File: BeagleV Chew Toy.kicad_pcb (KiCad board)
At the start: 2 copper layers, 41.1 x 51.1 mm, 3 parts

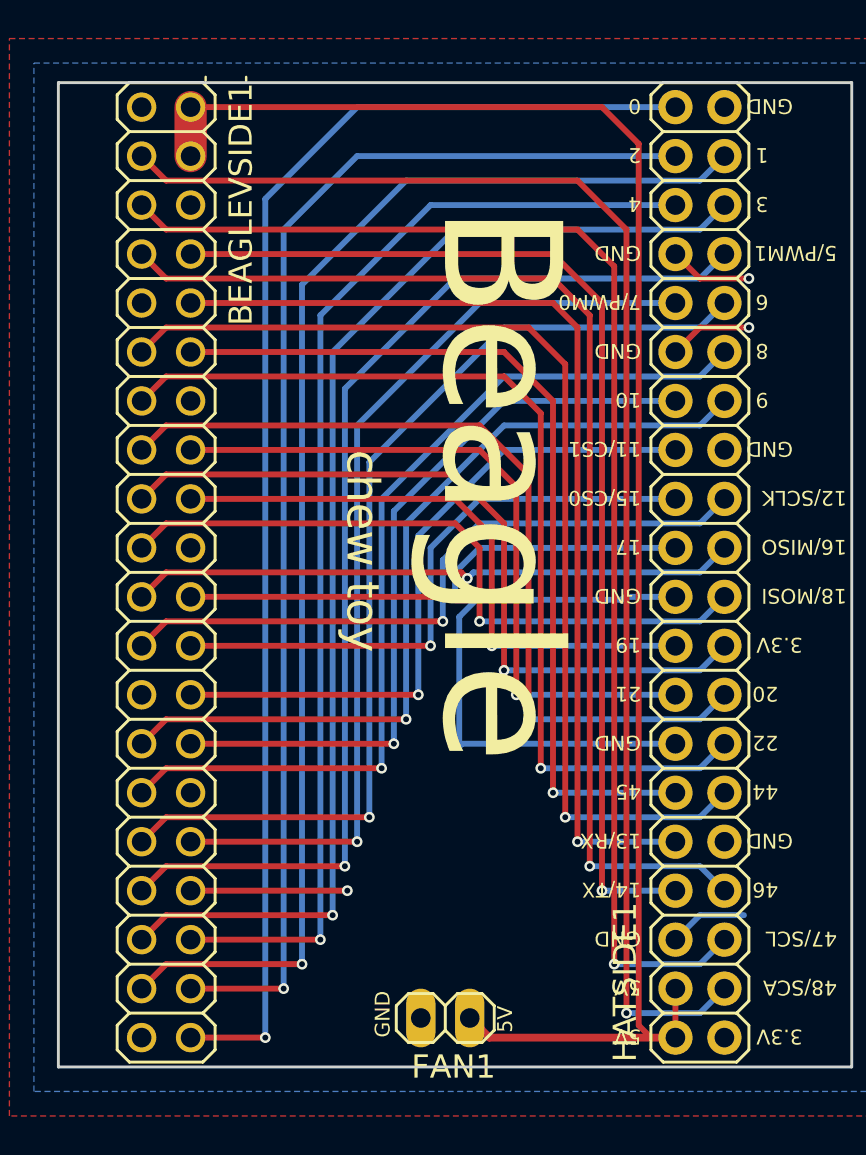
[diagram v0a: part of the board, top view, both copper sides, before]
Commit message: replace connectors
The footprints aren't the same anyway so let's use the Kicad parts.
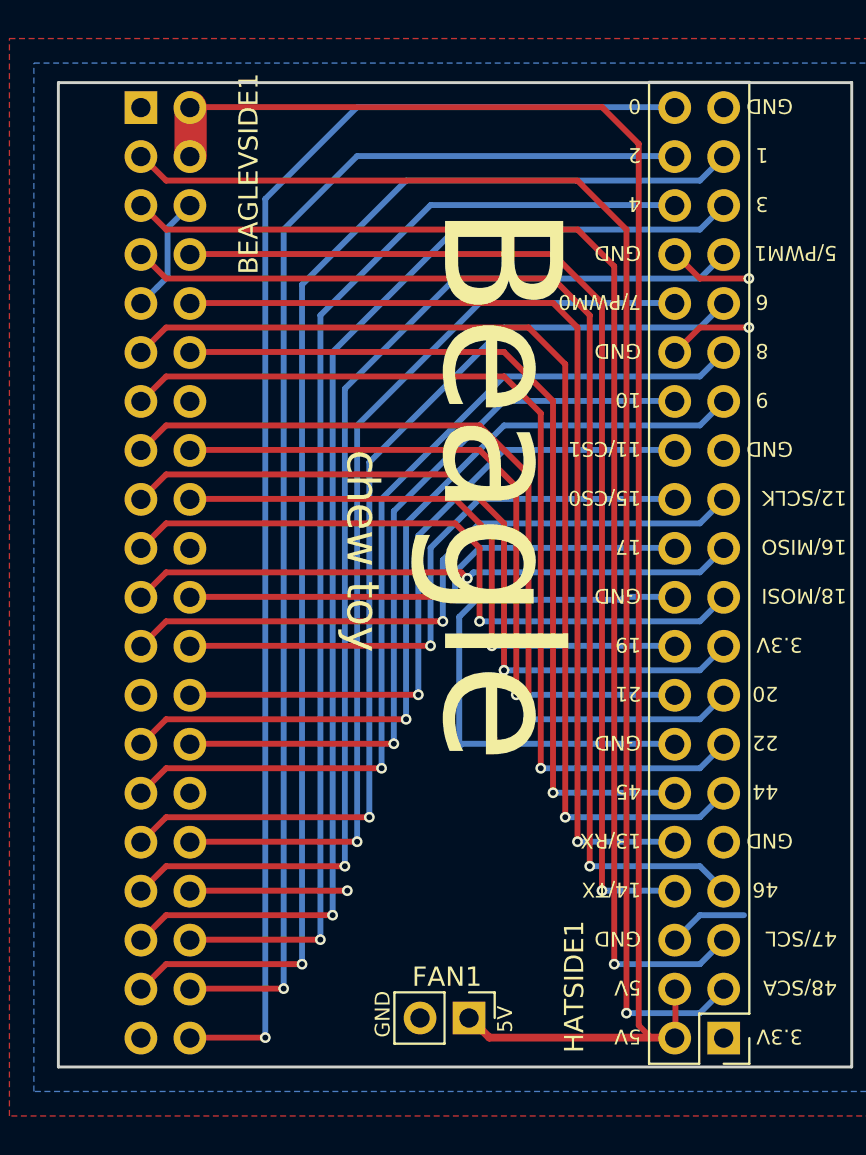
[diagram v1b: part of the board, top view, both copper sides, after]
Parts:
- BEAGLEVSIDE1: footprint BeagleV Chew Toy:2X20 -> Connector_PinSocket_2.54mm:PinSocket_2x20_P2.54mm_Vertical; moved to B.Cu
- FAN1: footprint BeagleV Chew Toy:1X02 -> Connector_PinHeader_2.54mm:PinHeader_1x02_P2.54mm_Vertical
- HATSIDE1: footprint BeagleV Chew Toy:2X20-BIG -> Connector_PinHeader_2.54mm:PinHeader_2x20_P2.54mm_Vertical
- moved HATSIDE1 24.2 mm to (162.4, 129.0), turned to 180 degrees
- moved BEAGLEVSIDE1 24.1 mm to (132.2, 80.8), turned to 180 degrees
- moved FAN1 1.23 mm to (149.2, 128.0), turned to 270 degrees
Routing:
- net /GND: track 50.5 -> 56.6 mm

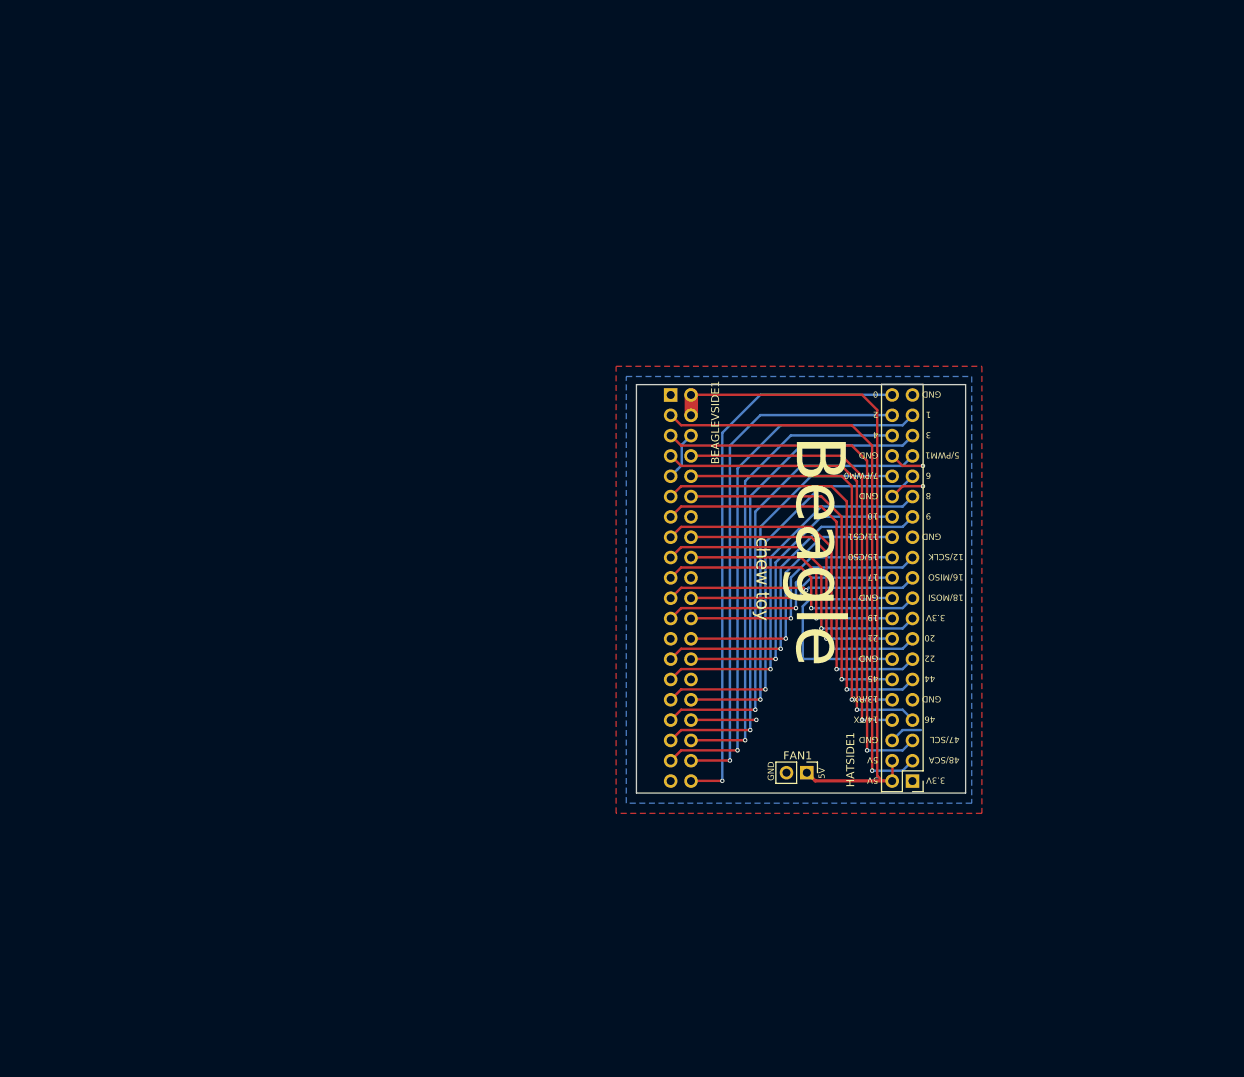
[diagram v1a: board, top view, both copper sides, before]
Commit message: add most of the parts that we need
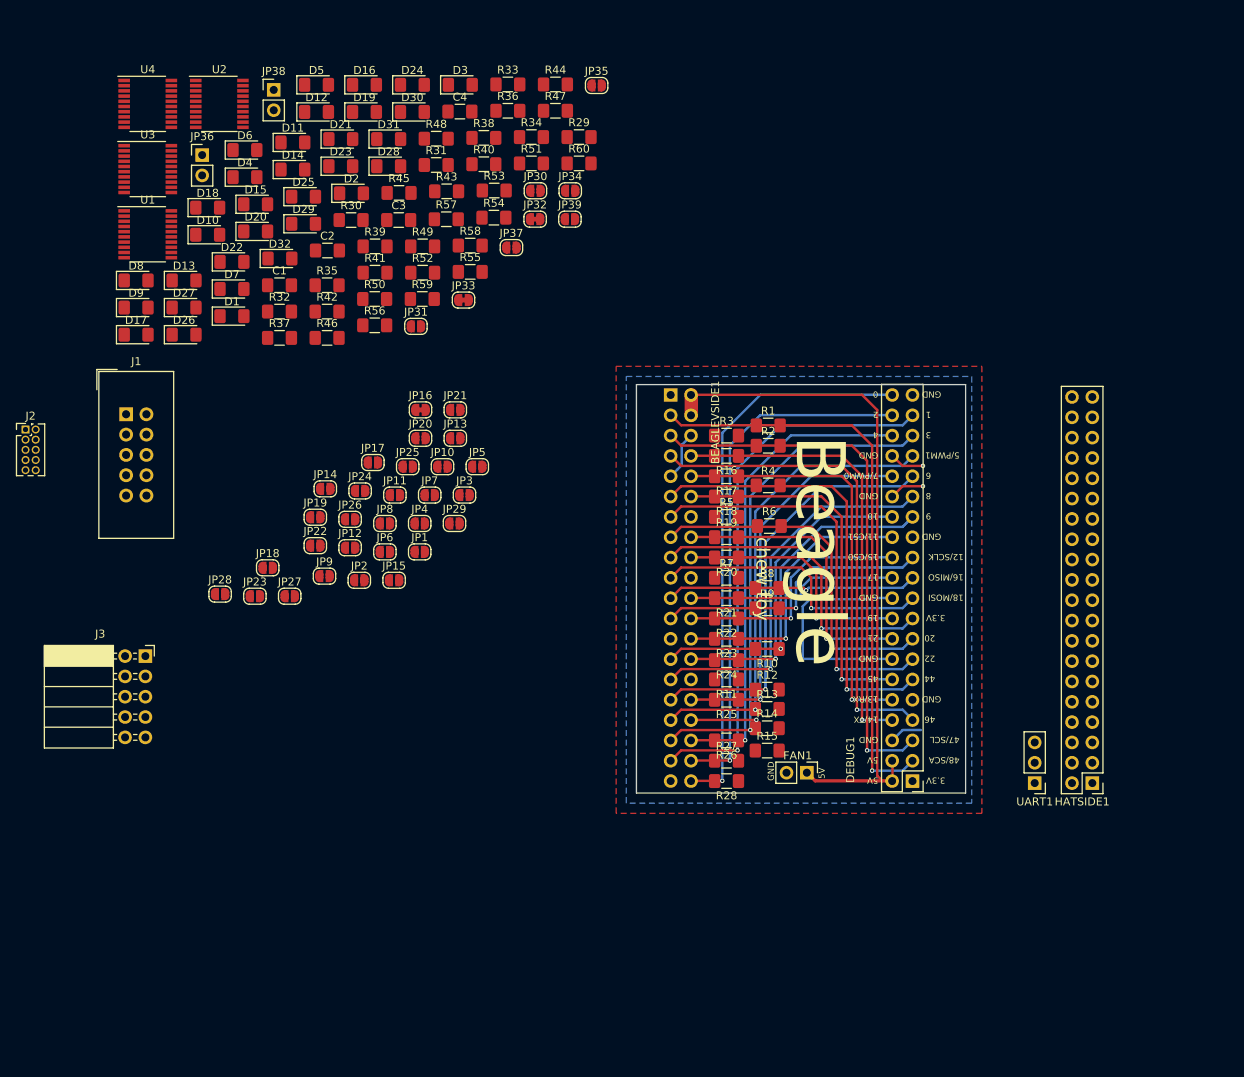
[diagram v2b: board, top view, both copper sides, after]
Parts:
- added C1: 100n, Capacitor_SMD:C_1206_3216Metric_Pad1.42x1.75mm_HandSolder, F.Cu at (83.3, 67.1)
- added C2: 100n, Capacitor_SMD:C_1206_3216Metric_Pad1.42x1.75mm_HandSolder, F.Cu at (89.3, 62.7)
- added C3: 100n, Capacitor_SMD:C_1206_3216Metric_Pad1.42x1.75mm_HandSolder, F.Cu at (98.2, 58.9)
- added C4: 100n, Capacitor_SMD:C_1206_3216Metric_Pad1.42x1.75mm_HandSolder, F.Cu at (105.9, 45.3)
- added D1: LED, LED_SMD:LED_1206_3216Metric_Pad1.42x1.75mm_HandSolder, F.Cu at (77.4, 70.9)
- added D10: LED, LED_SMD:LED_1206_3216Metric_Pad1.42x1.75mm_HandSolder, F.Cu at (74.3, 60.7)
- added D11: LED, LED_SMD:LED_1206_3216Metric_Pad1.42x1.75mm_HandSolder, F.Cu at (85.0, 49.2)
- added D12: LED, LED_SMD:LED_1206_3216Metric_Pad1.42x1.75mm_HandSolder, F.Cu at (87.9, 45.4)
- added D13: LED, LED_SMD:LED_1206_3216Metric_Pad1.42x1.75mm_HandSolder, F.Cu at (71.4, 66.5)
- added D14: LED, LED_SMD:LED_1206_3216Metric_Pad1.42x1.75mm_HandSolder, F.Cu at (85.0, 52.6)
- added D15: LED, LED_SMD:LED_1206_3216Metric_Pad1.42x1.75mm_HandSolder, F.Cu at (80.3, 56.9)
- added D16: LED, LED_SMD:LED_1206_3216Metric_Pad1.42x1.75mm_HandSolder, F.Cu at (93.9, 42.0)
- added D17: LED, LED_SMD:LED_1206_3216Metric_Pad1.42x1.75mm_HandSolder, F.Cu at (65.4, 73.2)
- added D18: LED, LED_SMD:LED_1206_3216Metric_Pad1.42x1.75mm_HandSolder, F.Cu at (74.3, 57.4)
- added D19: LED, LED_SMD:LED_1206_3216Metric_Pad1.42x1.75mm_HandSolder, F.Cu at (93.9, 45.4)
- added D2: LED, LED_SMD:LED_1206_3216Metric_Pad1.42x1.75mm_HandSolder, F.Cu at (92.3, 55.6)
- added D20: LED, LED_SMD:LED_1206_3216Metric_Pad1.42x1.75mm_HandSolder, F.Cu at (80.3, 60.3)
- added D21: LED, LED_SMD:LED_1206_3216Metric_Pad1.42x1.75mm_HandSolder, F.Cu at (91.0, 48.8)
- added D22: LED, LED_SMD:LED_1206_3216Metric_Pad1.42x1.75mm_HandSolder, F.Cu at (77.4, 64.1)
- added D23: LED, LED_SMD:LED_1206_3216Metric_Pad1.42x1.75mm_HandSolder, F.Cu at (91.0, 52.2)
- added D24: LED, LED_SMD:LED_1206_3216Metric_Pad1.42x1.75mm_HandSolder, F.Cu at (99.9, 42.0)
- added D25: LED, LED_SMD:LED_1206_3216Metric_Pad1.42x1.75mm_HandSolder, F.Cu at (86.3, 56.0)
- added D26: LED, LED_SMD:LED_1206_3216Metric_Pad1.42x1.75mm_HandSolder, F.Cu at (71.4, 73.2)
- added D27: LED, LED_SMD:LED_1206_3216Metric_Pad1.42x1.75mm_HandSolder, F.Cu at (71.4, 69.8)
- added D28: LED, LED_SMD:LED_1206_3216Metric_Pad1.42x1.75mm_HandSolder, F.Cu at (97.0, 52.2)
- added D29: LED, LED_SMD:LED_1206_3216Metric_Pad1.42x1.75mm_HandSolder, F.Cu at (86.3, 59.4)
- added D3: LED, LED_SMD:LED_1206_3216Metric_Pad1.42x1.75mm_HandSolder, F.Cu at (105.9, 42.0)
- added D30: LED, LED_SMD:LED_1206_3216Metric_Pad1.42x1.75mm_HandSolder, F.Cu at (99.9, 45.4)
- added D31: LED, LED_SMD:LED_1206_3216Metric_Pad1.42x1.75mm_HandSolder, F.Cu at (97.0, 48.8)
- added D32: LED, LED_SMD:LED_1206_3216Metric_Pad1.42x1.75mm_HandSolder, F.Cu at (83.4, 63.7)
- added D4: LED, LED_SMD:LED_1206_3216Metric_Pad1.42x1.75mm_HandSolder, F.Cu at (79.0, 53.5)
- added D5: LED, LED_SMD:LED_1206_3216Metric_Pad1.42x1.75mm_HandSolder, F.Cu at (87.9, 42.0)
- added D6: LED, LED_SMD:LED_1206_3216Metric_Pad1.42x1.75mm_HandSolder, F.Cu at (79.0, 50.2)
- added D7: LED, LED_SMD:LED_1206_3216Metric_Pad1.42x1.75mm_HandSolder, F.Cu at (77.4, 67.5)
- added D8: LED, LED_SMD:LED_1206_3216Metric_Pad1.42x1.75mm_HandSolder, F.Cu at (65.4, 66.5)
- added D9: LED, LED_SMD:LED_1206_3216Metric_Pad1.42x1.75mm_HandSolder, F.Cu at (65.4, 69.8)
- added HATSIDE1: PINHD-2X20-BIG, Connector_PinHeader_2.54mm:PinHeader_2x20_P2.54mm_Vertical, F.Cu at (184.9, 129.3)
- added J1: Conn_02x05_Counter_Clockwise, Connector_IDC:IDC-Header_2x05_P2.54mm_Vertical, F.Cu at (64.1, 83.2)
- added J2: Conn_02x05_Counter_Clockwise, Connector_PinHeader_1.27mm:PinHeader_2x05_P1.27mm_Vertical, F.Cu at (51.6, 85.1)
- added J3: Conn_02x05_Counter_Clockwise, Connector_PinSocket_2.54mm:PinSocket_2x05_P2.54mm_Horizontal, F.Cu at (66.5, 113.4)
- added JP1: SolderJumper_2_Bridged, Jumper:SolderJumper-2_P1.3mm_Open_RoundedPad1.0x1.5mm, F.Cu at (100.8, 100.4)
- added JP10: SolderJumper_2_Bridged, Jumper:SolderJumper-2_P1.3mm_Open_RoundedPad1.0x1.5mm, F.Cu at (103.7, 89.7)
- added JP11: SolderJumper_2_Bridged, Jumper:SolderJumper-2_P1.3mm_Open_RoundedPad1.0x1.5mm, F.Cu at (97.7, 93.3)
- added JP12: SolderJumper_2_Bridged, Jumper:SolderJumper-2_P1.3mm_Open_RoundedPad1.0x1.5mm, F.Cu at (92.1, 99.9)
- added JP13: SolderJumper_2_Bridged, Jumper:SolderJumper-2_P1.3mm_Open_RoundedPad1.0x1.5mm, F.Cu at (105.3, 86.2)
- added JP14: SolderJumper_2_Bridged, Jumper:SolderJumper-2_P1.3mm_Open_RoundedPad1.0x1.5mm, F.Cu at (89.0, 92.5)
- added JP15: SolderJumper_2_Bridged, Jumper:SolderJumper-2_P1.3mm_Open_RoundedPad1.0x1.5mm, F.Cu at (97.6, 103.9)
- added JP16: SolderJumper_2_Bridged, Jumper:SolderJumper-2_P1.3mm_Bridged_RoundedPad1.0x1.5mm, F.Cu at (100.9, 82.6)
- added JP17: SolderJumper_2_Bridged, Jumper:SolderJumper-2_P1.3mm_Open_RoundedPad1.0x1.5mm, F.Cu at (95.0, 89.2)
- added JP18: SolderJumper_2_Bridged, Jumper:SolderJumper-2_P1.3mm_Open_RoundedPad1.0x1.5mm, F.Cu at (81.8, 102.4)
- added JP19: SolderJumper_2_Bridged, Jumper:SolderJumper-2_P1.3mm_Open_RoundedPad1.0x1.5mm, F.Cu at (87.8, 96.1)
- added JP2: SolderJumper_2_Bridged, Jumper:SolderJumper-2_P1.3mm_Open_RoundedPad1.0x1.5mm, F.Cu at (93.3, 103.9)
- added JP20: SolderJumper_2_Bridged, Jumper:SolderJumper-2_P1.3mm_Open_RoundedPad1.0x1.5mm, F.Cu at (100.9, 86.2)
- added JP21: SolderJumper_2_Bridged, Jumper:SolderJumper-2_P1.3mm_Open_RoundedPad1.0x1.5mm, F.Cu at (105.3, 82.6)
- added JP22: SolderJumper_2_Bridged, Jumper:SolderJumper-2_P1.3mm_Open_RoundedPad1.0x1.5mm, F.Cu at (87.8, 99.6)
- added JP23: SolderJumper_2_Bridged, Jumper:SolderJumper-2_P1.3mm_Open_RoundedPad1.0x1.5mm, F.Cu at (80.2, 105.9)
- added JP24: SolderJumper_2_Bridged, Jumper:SolderJumper-2_P1.3mm_Open_RoundedPad1.0x1.5mm, F.Cu at (93.4, 92.8)
- added JP25: SolderJumper_2_Bridged, Jumper:SolderJumper-2_P1.3mm_Open_RoundedPad1.0x1.5mm, F.Cu at (99.3, 89.7)
- added JP26: SolderJumper_2_Bridged, Jumper:SolderJumper-2_P1.3mm_Open_RoundedPad1.0x1.5mm, F.Cu at (92.1, 96.3)
- added JP27: SolderJumper_2_Bridged, Jumper:SolderJumper-2_P1.3mm_Open_RoundedPad1.0x1.5mm, F.Cu at (84.6, 105.9)
- added JP28: SolderJumper_2_Bridged, Jumper:SolderJumper-2_P1.3mm_Open_RoundedPad1.0x1.5mm, F.Cu at (75.9, 105.7)
- added JP29: SolderJumper_2_Bridged, Jumper:SolderJumper-2_P1.3mm_Open_RoundedPad1.0x1.5mm, F.Cu at (105.2, 96.8)
- added JP3: SolderJumper_2_Bridged, Jumper:SolderJumper-2_P1.3mm_Open_RoundedPad1.0x1.5mm, F.Cu at (106.4, 93.3)
- added JP30: SolderJumper_2_Bridged, Jumper:SolderJumper-2_P1.3mm_Open_RoundedPad1.0x1.5mm, F.Cu at (115.3, 55.2)
- added JP31: SolderJumper_2_Bridged, Jumper:SolderJumper-2_P1.3mm_Open_RoundedPad1.0x1.5mm, F.Cu at (100.4, 72.2)
- added JP32: SolderJumper_2_Bridged, Jumper:SolderJumper-2_P1.3mm_Bridged_RoundedPad1.0x1.5mm, F.Cu at (115.3, 58.8)
- added JP33: SolderJumper_2_Bridged, Jumper:SolderJumper-2_P1.3mm_Bridged_RoundedPad1.0x1.5mm, F.Cu at (106.3, 68.9)
- added JP34: SolderJumper_2_Bridged, Jumper:SolderJumper-2_P1.3mm_Open_RoundedPad1.0x1.5mm, F.Cu at (119.7, 55.2)
- added JP35: SolderJumper_2_Bridged, Jumper:SolderJumper-2_P1.3mm_Open_RoundedPad1.0x1.5mm, F.Cu at (123.0, 42.1)
- added JP36: Jumper, Connector_PinHeader_2.54mm:PinHeader_1x02_P2.54mm_Vertical, F.Cu at (73.6, 50.8)
- added JP37: SolderJumper_2_Bridged, Jumper:SolderJumper-2_P1.3mm_Open_RoundedPad1.0x1.5mm, F.Cu at (112.3, 62.3)
- added JP38: Jumper, Connector_PinHeader_2.54mm:PinHeader_1x02_P2.54mm_Vertical, F.Cu at (82.6, 42.6)
- added JP39: SolderJumper_2_Bridged, Jumper:SolderJumper-2_P1.3mm_Open_RoundedPad1.0x1.5mm, F.Cu at (119.6, 58.8)
- added JP4: SolderJumper_2_Bridged, Jumper:SolderJumper-2_P1.3mm_Open_RoundedPad1.0x1.5mm, F.Cu at (100.8, 96.8)
- added JP5: SolderJumper_2_Bridged, Jumper:SolderJumper-2_P1.3mm_Open_RoundedPad1.0x1.5mm, F.Cu at (108.0, 89.7)
- added JP6: SolderJumper_2_Bridged, Jumper:SolderJumper-2_P1.3mm_Open_RoundedPad1.0x1.5mm, F.Cu at (96.5, 100.4)
- added JP7: SolderJumper_2_Bridged, Jumper:SolderJumper-2_P1.3mm_Open_RoundedPad1.0x1.5mm, F.Cu at (102.1, 93.3)
- added JP8: SolderJumper_2_Bridged, Jumper:SolderJumper-2_P1.3mm_Open_RoundedPad1.0x1.5mm, F.Cu at (96.5, 96.8)
- added JP9: SolderJumper_2_Bridged, Jumper:SolderJumper-2_P1.3mm_Open_RoundedPad1.0x1.5mm, F.Cu at (88.9, 103.4)
- added R1: 100R, Resistor_SMD:R_1206_3216Metric_Pad1.42x1.75mm_HandSolder, F.Cu at (144.4, 84.6)
- added R10: 100R, Resistor_SMD:R_1206_3216Metric_Pad1.42x1.75mm_HandSolder, F.Cu at (144.3, 112.5)
- added R11: 100R, Resistor_SMD:R_1206_3216Metric_Pad1.42x1.75mm_HandSolder, F.Cu at (139.2, 116.3)
- added R12: 100R, Resistor_SMD:R_1206_3216Metric_Pad1.42x1.75mm_HandSolder, F.Cu at (144.3, 117.6)
- added R13: 100R, Resistor_SMD:R_1206_3216Metric_Pad1.42x1.75mm_HandSolder, F.Cu at (144.3, 120.0)
- added R14: 100R, Resistor_SMD:R_1206_3216Metric_Pad1.42x1.75mm_HandSolder, F.Cu at (144.3, 122.4)
- added R15: 100R, Resistor_SMD:R_1206_3216Metric_Pad1.42x1.75mm_HandSolder, F.Cu at (144.3, 125.2)
- added R16: 100R, Resistor_SMD:R_1206_3216Metric_Pad1.42x1.75mm_HandSolder, F.Cu at (139.2, 88.4)
- added R17: 100R, Resistor_SMD:R_1206_3216Metric_Pad1.42x1.75mm_HandSolder, F.Cu at (139.2, 90.9)
- added R18: 100R, Resistor_SMD:R_1206_3216Metric_Pad1.42x1.75mm_HandSolder, F.Cu at (139.2, 93.5)
- added R19: 100R, Resistor_SMD:R_1206_3216Metric_Pad1.42x1.75mm_HandSolder, F.Cu at (139.2, 98.6)
- added R2: 100R, Resistor_SMD:R_1206_3216Metric_Pad1.42x1.75mm_HandSolder, F.Cu at (144.4, 87.1)
- added R20: 100R, Resistor_SMD:R_1206_3216Metric_Pad1.42x1.75mm_HandSolder, F.Cu at (139.2, 101.1)
- added R21: 100R, Resistor_SMD:R_1206_3216Metric_Pad1.42x1.75mm_HandSolder, F.Cu at (139.2, 106.2)
- added R22: 100R, Resistor_SMD:R_1206_3216Metric_Pad1.42x1.75mm_HandSolder, F.Cu at (139.2, 108.7)
- added R23: 100R, Resistor_SMD:R_1206_3216Metric_Pad1.42x1.75mm_HandSolder, F.Cu at (139.2, 111.3)
- added R24: 100R, Resistor_SMD:R_1206_3216Metric_Pad1.42x1.75mm_HandSolder, F.Cu at (139.2, 113.9)
- added R25: 100R, Resistor_SMD:R_1206_3216Metric_Pad1.42x1.75mm_HandSolder, F.Cu at (139.2, 118.9)
- added R26: 100R, Resistor_SMD:R_1206_3216Metric_Pad1.42x1.75mm_HandSolder, F.Cu at (139.2, 124.0)
- added R27: 100R, Resistor_SMD:R_1206_3216Metric_Pad1.42x1.75mm_HandSolder, F.Cu at (139.2, 126.5)
- added R28: 100R, Resistor_SMD:R_1206_3216Metric_Pad1.42x1.75mm_HandSolder, F.Cu at (139.2, 129.0)
- added R29: 1k, Resistor_SMD:R_1206_3216Metric_Pad1.42x1.75mm_HandSolder, F.Cu at (120.8, 48.5)
- added R3: 100R, Resistor_SMD:R_1206_3216Metric_Pad1.42x1.75mm_HandSolder, F.Cu at (139.2, 85.9)
- added R30: 1k, Resistor_SMD:R_1206_3216Metric_Pad1.42x1.75mm_HandSolder, F.Cu at (92.3, 58.9)
- added R31: 1k, Resistor_SMD:R_1206_3216Metric_Pad1.42x1.75mm_HandSolder, F.Cu at (102.9, 52.0)
- added R32: 1k, Resistor_SMD:R_1206_3216Metric_Pad1.42x1.75mm_HandSolder, F.Cu at (83.3, 70.3)
- added R33: 1k, Resistor_SMD:R_1206_3216Metric_Pad1.42x1.75mm_HandSolder, F.Cu at (111.9, 42.0)
- added R34: 1k, Resistor_SMD:R_1206_3216Metric_Pad1.42x1.75mm_HandSolder, F.Cu at (114.8, 48.5)
- added R35: 1k, Resistor_SMD:R_1206_3216Metric_Pad1.42x1.75mm_HandSolder, F.Cu at (89.3, 67.1)
- added R36: 1k, Resistor_SMD:R_1206_3216Metric_Pad1.42x1.75mm_HandSolder, F.Cu at (111.9, 45.2)
- added R37: 1k, Resistor_SMD:R_1206_3216Metric_Pad1.42x1.75mm_HandSolder, F.Cu at (83.3, 73.6)
- added R38: 1k, Resistor_SMD:R_1206_3216Metric_Pad1.42x1.75mm_HandSolder, F.Cu at (108.9, 48.6)
- added R39: 1k, Resistor_SMD:R_1206_3216Metric_Pad1.42x1.75mm_HandSolder, F.Cu at (95.3, 62.2)
- added R4: 100R, Resistor_SMD:R_1206_3216Metric_Pad1.42x1.75mm_HandSolder, F.Cu at (144.4, 92.1)
- added R40: 1k, Resistor_SMD:R_1206_3216Metric_Pad1.42x1.75mm_HandSolder, F.Cu at (108.9, 51.9)
- added R41: 1k, Resistor_SMD:R_1206_3216Metric_Pad1.42x1.75mm_HandSolder, F.Cu at (95.3, 65.5)
- added R42: 1k, Resistor_SMD:R_1206_3216Metric_Pad1.42x1.75mm_HandSolder, F.Cu at (89.3, 70.3)
- added R43: 1k, Resistor_SMD:R_1206_3216Metric_Pad1.42x1.75mm_HandSolder, F.Cu at (104.2, 55.3)
- added R44: 1k, Resistor_SMD:R_1206_3216Metric_Pad1.42x1.75mm_HandSolder, F.Cu at (117.8, 42.0)
- added R45: 1k, Resistor_SMD:R_1206_3216Metric_Pad1.42x1.75mm_HandSolder, F.Cu at (98.3, 55.5)
- added R46: 1k, Resistor_SMD:R_1206_3216Metric_Pad1.42x1.75mm_HandSolder, F.Cu at (89.3, 73.6)
- added R47: 1k, Resistor_SMD:R_1206_3216Metric_Pad1.42x1.75mm_HandSolder, F.Cu at (117.8, 45.2)
- added R48: 1k, Resistor_SMD:R_1206_3216Metric_Pad1.42x1.75mm_HandSolder, F.Cu at (102.9, 48.7)
- added R49: 1k, Resistor_SMD:R_1206_3216Metric_Pad1.42x1.75mm_HandSolder, F.Cu at (101.2, 62.2)
- added R5: 100R, Resistor_SMD:R_1206_3216Metric_Pad1.42x1.75mm_HandSolder, F.Cu at (139.2, 96.0)
- added R50: 1k, Resistor_SMD:R_1206_3216Metric_Pad1.42x1.75mm_HandSolder, F.Cu at (95.2, 68.8)
- added R51: 1k, Resistor_SMD:R_1206_3216Metric_Pad1.42x1.75mm_HandSolder, F.Cu at (114.8, 51.8)
- added R52: 1k, Resistor_SMD:R_1206_3216Metric_Pad1.42x1.75mm_HandSolder, F.Cu at (101.2, 65.5)
- added R53: 1k, Resistor_SMD:R_1206_3216Metric_Pad1.42x1.75mm_HandSolder, F.Cu at (110.2, 55.2)
- added R54: 1k, Resistor_SMD:R_1206_3216Metric_Pad1.42x1.75mm_HandSolder, F.Cu at (110.1, 58.6)
- added R55: 1k, Resistor_SMD:R_1206_3216Metric_Pad1.42x1.75mm_HandSolder, F.Cu at (107.2, 65.4)
- added R56: 1k, Resistor_SMD:R_1206_3216Metric_Pad1.42x1.75mm_HandSolder, F.Cu at (95.2, 72.1)
- added R57: 1k, Resistor_SMD:R_1206_3216Metric_Pad1.42x1.75mm_HandSolder, F.Cu at (104.2, 58.8)
- added R58: 1k, Resistor_SMD:R_1206_3216Metric_Pad1.42x1.75mm_HandSolder, F.Cu at (107.2, 62.1)
- added R59: 1k, Resistor_SMD:R_1206_3216Metric_Pad1.42x1.75mm_HandSolder, F.Cu at (101.2, 68.8)
- added R6: 100R, Resistor_SMD:R_1206_3216Metric_Pad1.42x1.75mm_HandSolder, F.Cu at (144.5, 97.2)
- added R60: 1k, Resistor_SMD:R_1206_3216Metric_Pad1.42x1.75mm_HandSolder, F.Cu at (120.8, 51.8)
- added R7: 100R, Resistor_SMD:R_1206_3216Metric_Pad1.42x1.75mm_HandSolder, F.Cu at (139.2, 103.6)
- added R8: 100R, Resistor_SMD:R_1206_3216Metric_Pad1.42x1.75mm_HandSolder, F.Cu at (144.3, 104.9)
- added R9: 100R, Resistor_SMD:R_1206_3216Metric_Pad1.42x1.75mm_HandSolder, F.Cu at (144.3, 107.4)
- added U1: 74HC245, Package_SO:TSSOP-20_4.4x6.5mm_P0.65mm, F.Cu at (66.8, 60.7)
- added U2: 74HC245, Package_SO:TSSOP-20_4.4x6.5mm_P0.65mm, F.Cu at (75.8, 44.4)
- added U3: 74HC245, Package_SO:TSSOP-20_4.4x6.5mm_P0.65mm, F.Cu at (66.8, 52.5)
- added U4: 74HC245, Package_SO:TSSOP-20_4.4x6.5mm_P0.65mm, F.Cu at (66.8, 44.4)
- added UART1: PINHD-1X2, Connector_PinHeader_2.54mm:PinHeader_1x03_P2.54mm_Vertical, F.Cu at (177.7, 129.3)
- renumbered HATSIDE1 to DEBUG1
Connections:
- net /3.3V renamed +3V3
- net /5V renamed +5V
- net /GND renamed GND
- BEAGLEVSIDE1 pad 10: /GPIO13/RX -> Net-(BEAGLEVSIDE1-Pad10)
- BEAGLEVSIDE1 pad 11: /GPIO44 -> Net-(BEAGLEVSIDE1-Pad11)
- BEAGLEVSIDE1 pad 12: /GPIO45 -> Net-(BEAGLEVSIDE1-Pad12)
- BEAGLEVSIDE1 pad 13: /GPIO22 -> Net-(BEAGLEVSIDE1-Pad13)
- BEAGLEVSIDE1 pad 15: /GPIO20 -> Net-(BEAGLEVSIDE1-Pad15)
- BEAGLEVSIDE1 pad 16: /GPIO21 -> Net-(BEAGLEVSIDE1-Pad16)
- BEAGLEVSIDE1 pad 18: /GPIO19 -> Net-(BEAGLEVSIDE1-Pad18)
- BEAGLEVSIDE1 pad 19: /GPIO18/MOSI -> Net-(BEAGLEVSIDE1-Pad19)
- BEAGLEVSIDE1 pad 21: /GPIO16/MISO -> Net-(BEAGLEVSIDE1-Pad21)
- BEAGLEVSIDE1 pad 22: /GPIO17 -> Net-(BEAGLEVSIDE1-Pad22)
- BEAGLEVSIDE1 pad 23: /GPIO12/SCLK -> Net-(BEAGLEVSIDE1-Pad23)
- BEAGLEVSIDE1 pad 24: /GPIO15/CS0 -> Net-(BEAGLEVSIDE1-Pad24)
- BEAGLEVSIDE1 pad 26: /GPIO11/CS1 -> Net-(BEAGLEVSIDE1-Pad26)
- BEAGLEVSIDE1 pad 27: /GPIO9 -> Net-(BEAGLEVSIDE1-Pad27)
- BEAGLEVSIDE1 pad 28: /GPIO10 -> Net-(BEAGLEVSIDE1-Pad28)
- BEAGLEVSIDE1 pad 29: /GPIO8 -> Net-(BEAGLEVSIDE1-Pad29)
- BEAGLEVSIDE1 pad 3: /GPIO48/SDA -> Net-(BEAGLEVSIDE1-Pad3)
- BEAGLEVSIDE1 pad 31: /GPIO6 -> Net-(BEAGLEVSIDE1-Pad31)
- BEAGLEVSIDE1 pad 32: /GPIO7/PWM -> Net-(BEAGLEVSIDE1-Pad32)
- BEAGLEVSIDE1 pad 33: /GPIO5/PWM -> Net-(BEAGLEVSIDE1-Pad33)
- BEAGLEVSIDE1 pad 35: /GPIO3 -> Net-(BEAGLEVSIDE1-Pad35)
- BEAGLEVSIDE1 pad 36: /GPIO4 -> Net-(BEAGLEVSIDE1-Pad36)
- BEAGLEVSIDE1 pad 37: /GPIO1 -> Net-(BEAGLEVSIDE1-Pad37)
- BEAGLEVSIDE1 pad 38: /GPIO2 -> Net-(BEAGLEVSIDE1-Pad38)
- BEAGLEVSIDE1 pad 40: /GPIO0 -> Net-(BEAGLEVSIDE1-Pad40)
- BEAGLEVSIDE1 pad 5: /GPIO47/SCL -> Net-(BEAGLEVSIDE1-Pad5)
- BEAGLEVSIDE1 pad 7: /GPIO46 -> Net-(BEAGLEVSIDE1-Pad7)
- BEAGLEVSIDE1 pad 8: /GPIO14/TX -> Net-(BEAGLEVSIDE1-Pad8)

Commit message: place LEDs and resistors
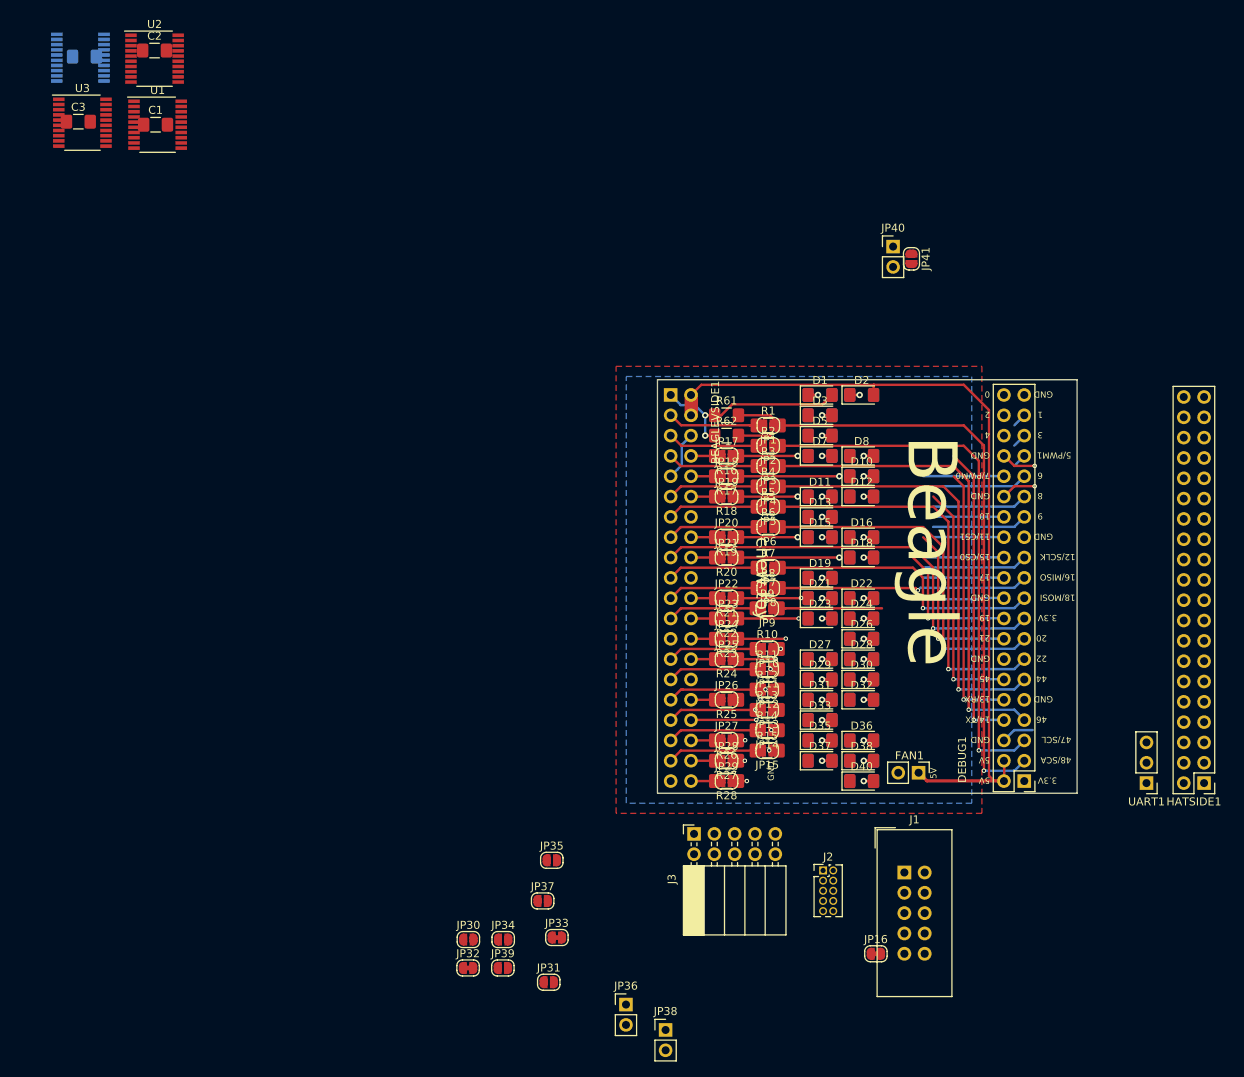
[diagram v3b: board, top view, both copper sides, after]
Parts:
- removed D6: LED, LED_SMD:LED_1206_3216Metric_Pad1.42x1.75mm_HandSolder
- removed R29, R30, R34: 1k, Resistor_SMD:R_1206_3216Metric_Pad1.42x1.75mm_HandSolder
- added JP40: Jumper, Connector_PinHeader_2.54mm:PinHeader_1x02_P2.54mm_Vertical, F.Cu at (160.0, 62.2)
- added JP41: SolderJumper_2_Bridged, Jumper:SolderJumper-2_P1.3mm_Open_RoundedPad1.0x1.5mm, F.Cu at (162.3, 63.8)
- added R61: 4k7, Resistor_SMD:R_1206_3216Metric_Pad1.42x1.75mm_HandSolder, F.Cu at (139.2, 83.3)
- added R62: 4k7, Resistor_SMD:R_1206_3216Metric_Pad1.42x1.75mm_HandSolder, F.Cu at (139.2, 85.9)
- added R63: 1k, Resistor_SMD:R_1206_3216Metric_Pad1.42x1.75mm_HandSolder, B.Cu at (150.9, 80.8)
- added R64: 1k, Resistor_SMD:R_1206_3216Metric_Pad1.42x1.75mm_HandSolder, B.Cu at (156.1, 80.8)
- C4, R31, R32, R33, R35, R36, R37, R38, R39, R40, R41, R42, R43, R44, R45, R46, R47, R48, R49, R50, R51, R52, R53, R54, R55, R56, R57, R58, R59, R60, U4: moved to B.Cu
- moved JP38 127.3 mm to (131.6, 160.1)
- moved JP36 118.7 mm to (126.6, 157.0)
- moved J2 113.9 mm to (151.3, 140.2)
- moved J1 112.9 mm to (161.4, 140.5)
- moved D40 107.9 mm to (156.1, 129.0)
- moved D36 100.7 mm to (156.1, 124.0)
- moved D37 100.7 mm to (150.9, 126.5)
- moved D38 100.6 mm to (156.1, 126.5)
- moved D33 99.8 mm to (150.9, 121.4)
- moved JP35 97.0 mm to (117.3, 138.9)
- moved R48 94.2 mm to (156.1, 126.5)
- moved JP32 94.0 mm to (106.9, 152.4)
- moved JP39 94.0 mm to (111.2, 152.4)
- moved JP30 94.0 mm to (106.9, 148.8)
- moved JP34 94.0 mm to (111.3, 148.8)
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- renumbered D9 to D33, D25 to D35, D14 to D36, D17 to D37, D20 to D38, D4 to D40
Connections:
- D1 pad 1: GND -> Net-(D1-Pad1)
- D1 pad 2: Net-(D1-Pad2) -> +3V3
- D2 pad 1: GND -> Net-(D2-Pad1)
- D2 pad 2: Net-(D2-Pad2) -> +5V
- DEBUG1 pad 35: /GPIO3 -> /GPIO3_TMS
- DEBUG1 pad 36: /GPIO4 -> /GPIO4_TRSTN
- DEBUG1 pad 37: /GPIO1 -> /GPIO1_TCK
- DEBUG1 pad 38: /GPIO2 -> /GPIO2_TDI_TO_SOC
- DEBUG1 pad 40: /GPIO0 -> /GPIO0_TDO_FROM_SOC
- HATSIDE1 pad 35: /GPIO3 -> /GPIO3_TMS
- HATSIDE1 pad 36: /GPIO4 -> /GPIO4_TRSTN
- HATSIDE1 pad 37: /GPIO1 -> /GPIO1_TCK
- HATSIDE1 pad 38: /GPIO2 -> /GPIO2_TDI_TO_SOC
- HATSIDE1 pad 40: /GPIO0 -> /GPIO0_TDO_FROM_SOC
- JP30 pad 1: Net-(JP30-Pad1) -> Net-(J3-Pad2)
- JP30 pad 2: Net-(JP30-Pad2) -> +3V3
- JP31 pad 1: Net-(JP31-Pad1) -> Net-(J3-Pad4)
- JP31 pad 2: Net-(JP31-Pad2) -> +5V
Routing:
- net /GPIO0: track 70.6 -> 0.00 mm, vias 1 -> 0
- net /GPIO1: track 68.8 -> 0.00 mm, vias 1 -> 0
- net /GPIO2: track 66.7 -> 0.00 mm, vias 1 -> 0
- net /GPIO3: track 63.1 -> 0.00 mm, vias 1 -> 0
- net /GPIO4: track 60.5 -> 0.00 mm, vias 1 -> 0
- net /GPIO5/PWM: track 58.4 -> 2.63 mm, vias 1 -> 0
- net +3V3: track 40.0 -> 79.9 mm, vias 1 -> 3
- net /GPIO6: track 52.6 -> 12.8 mm, vias 1 -> 0
- net /GPIO7/PWM: track 49.4 -> 10.2 mm
- net /GPIO8: track 47.9 -> 12.8 mm
- net /GPIO9: track 43.5 -> 12.8 mm
- net /GPIO10: track 39.6 -> 14.4 mm
- net /GPIO11/CS1: track 35.2 -> 15.7 mm
- net GND: track 56.6 -> 37.4 mm
- net +5V: track 88.1 -> 104.4 mm
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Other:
- board size 41.1 x 51.1 mm -> 52.5 x 51.7 mm
